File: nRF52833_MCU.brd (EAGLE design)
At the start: 47.7 x 30.2 mm, 45 parts, among them IC1 SKY13415-485LF, J100 DEBUG_CONNECTOR, J3 282834-2, U1 nRF52833-QIAA, X1 32MHz, X2 32.768kHz, X3 22-23-2031

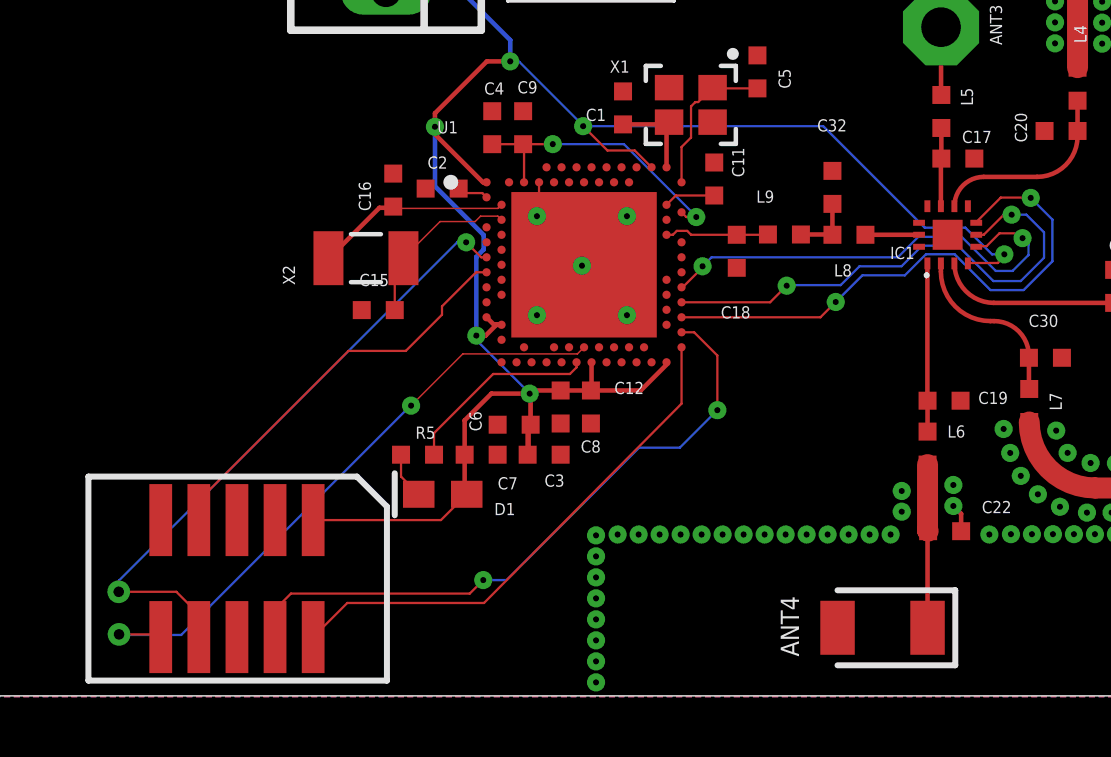
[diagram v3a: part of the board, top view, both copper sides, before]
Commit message: Disconnect reset
Signed-off-by: Florian Depraz <florian.depraz@outlook.com>
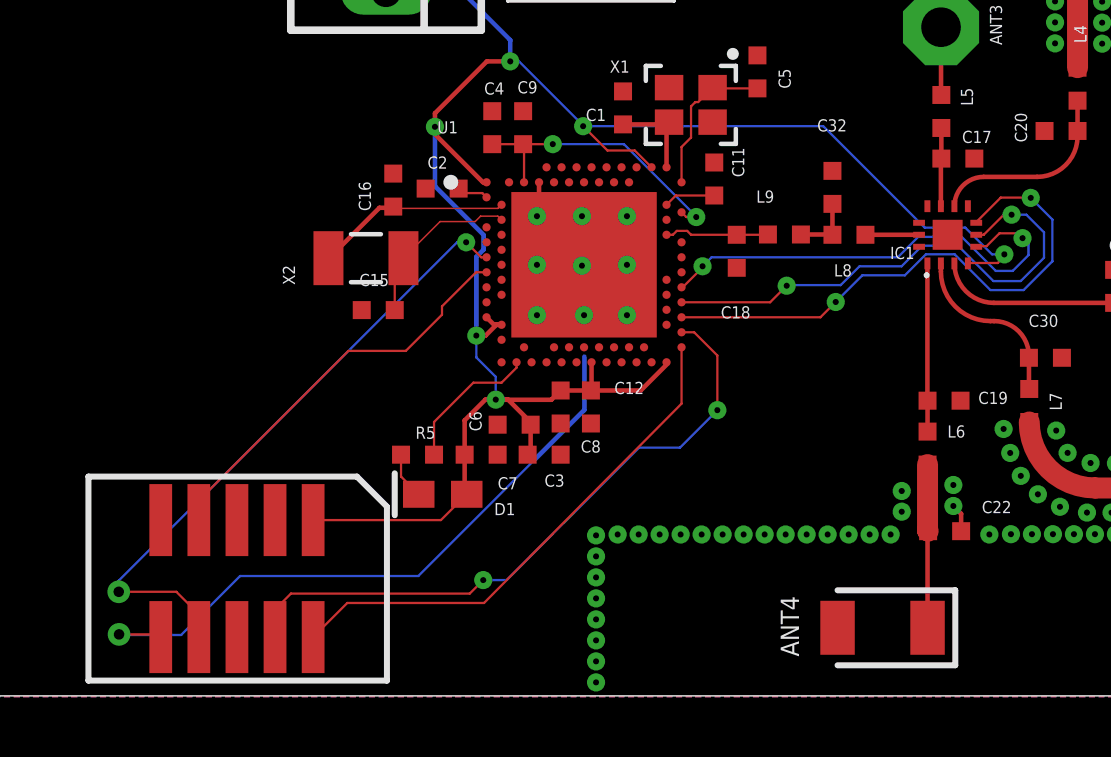
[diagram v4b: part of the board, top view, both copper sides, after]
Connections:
- net LED1: now also U1.AD4; no longer U1.AD12
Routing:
- net GND: track 3.13 -> 5.27 mm, vias 39 -> 43
- net VDD: track 68.9 -> 67.1 mm
- net LED1: track 6.55 -> 4.77 mm
- net RESET: track 20.9 -> 21.8 mm, vias 2 -> 1
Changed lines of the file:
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@@
 <signal name="LED1">
 <contactref element="R5" pad="1"/>
-<contactref element="U1" pad="AD12"/>
-<wire x1="30.07" y1="39.55" x2="30.07" y2="40.27" width="0.0762" layer="1"/>
-<wire x1="34.82" y1="42.63" x2="34.82" y2="42.46" width="0.0762" layer="1"/>
-<wire x1="34.82" y1="42.46" x2="34.6" y2="42.24" width="0.0762" layer="1"/>
-<wire x1="32.04" y1="42.24" x2="30.07" y2="40.27" width="0.0762" layer="1"/>
-<wire x1="34.6" y1="42.24" x2="32.04" y2="42.24" width="0.0762" layer="1"/>
+<wire x1="30.07" y1="39.55" x2="30.07" y2="40.64" width="0.0762" layer="1"/>
+<wire x1="31.38" y1="41.95" x2="30.07" y2="40.64" width="0.0762" layer="1"/>
+<wire x1="32.32" y1="41.95" x2="31.38" y2="41.95" width="0.0762" layer="1"/>
+<contactref element="U1" pad="AD4"/>
+<wire x1="32.820003125" y1="42.63" x2="32.820003125" y2="42.450003125" width="0.0762" layer="1"/>
+<wire x1="32.820003125" y1="42.450003125" x2="32.32" y2="41.95" width="0.0762" layer="1"/>
 </signal>
 <signal name="P0.07_RX">
@@
 <wire x1="35.04" y1="50.52" x2="32.91" y2="52.65" width="0.0762" layer="16"/>
 <via x="35.04" y="50.5" extent="1-16" drill="0.2"/>
-<wire x1="33.19" y1="39.55" x2="33.26" y2="39.62" width="0.0762" layer="1"/>
-<wire x1="33.2575" y1="41.5857" x2="33.26" y2="41.5832" width="0.0762" layer="1"/>
-<wire x1="33.26" y1="41.5832" x2="33.26" y2="39.62" width="0.0762" layer="1"/>
-<via x="33.2575" y="41.5857" extent="1-16" drill="0.2"/>
+<via x="32.1275" y="41.3857" extent="1-16" drill="0.2"/>
 <wire x1="37.820003125" y1="42.63" x2="37.820003125" y2="42.55" width="0.0762" layer="1"/>
 <wire x1="36.960003125" y1="41.69" x2="37.820003125" y2="42.55" width="0.1524" layer="1"/>
@@
 <contactref element="U1" pad="Y2"/>
 <via x="32.61" y="52.66" extent="1-16" drill="0.2"/>
-<wire x1="31.98190625" y1="41.5857" x2="33.2575" y2="41.5857" width="0.1524" layer="1"/>
+<wire x1="31.78190625" y1="41.3857" x2="32.1275" y2="41.3857" width="0.1524" layer="1"/>
 <wire x1="31.09" y1="39.55" x2="31.09" y2="40.69379375" width="0.1524" layer="1"/>
-<wire x1="31.09" y1="40.69379375" x2="31.98190625" y2="41.5857" width="0.1524" layer="1"/>
+<wire x1="31.09" y1="40.69379375" x2="31.78190625" y2="41.3857" width="0.1524" layer="1"/>
 <wire x1="35.320003125" y1="41.710003125" x2="35.320003125" y2="42.63" width="0.1524" layer="1"/>
 <wire x1="31.09" y1="39.55" x2="31.09" y2="38.3" width="0.1524" layer="1"/>
@@
 <wire x1="30.3" y1="37.37" x2="26.04" y2="37.37" width="0.0762" layer="1"/>
 <via x="31.479328125" y="43.520671875" extent="1-16" drill="0.2"/>
-<wire x1="33.2575" y1="41.5857" x2="33.2575" y2="41.5957" width="0.0762" layer="16"/>
-<wire x1="33.2575" y1="41.5957" x2="31.479328125" y2="43.373871875" width="0.0762" layer="16"/>
-<wire x1="31.479328125" y1="43.373871875" x2="31.479328125" y2="43.5" width="0.0762" layer="16"/>
+<wire x1="32.1275" y1="41.3857" x2="32.1275" y2="42.1457" width="0.0762" layer="16"/>
+<wire x1="32.1275" y1="42.1457" x2="31.479328125" y2="42.793871875" width="0.0762" layer="16"/>
+<wire x1="31.479328125" y1="42.793871875" x2="31.479328125" y2="43.5" width="0.0762" layer="16"/>
 <wire x1="31.479328125" y1="43.5" x2="31.479328125" y2="43.520671875" width="0.0762" layer="16"/>
 <wire x1="31.7244" y1="46.87206875" x2="31.7244" y2="46.38793125" width="0.1524" layer="16"/>
@@
 <wire x1="31.479328125" y1="46.142859375" x2="31.479328125" y2="43.5" width="0.1524" layer="16"/>
 <wire x1="32.61" y1="53.37" x2="32.61" y2="52.66" width="0.1524" layer="16"/>
-<wire x1="33.19" y1="39.55" x2="33.19" y2="40.45" width="0.1524" layer="1"/>
-<wire x1="33.19" y1="40.45" x2="33.29" y2="40.55" width="0.1524" layer="1"/>
-<wire x1="33.29" y1="40.55" x2="33.29" y2="41.5532" width="0.1524" layer="1"/>
-<wire x1="33.29" y1="41.5532" x2="33.2575" y2="41.5857" width="0.1524" layer="1"/>
+<wire x1="33.29" y1="40.55" x2="33.29" y2="39.65" width="0.1524" layer="1"/>
+<wire x1="33.29" y1="39.65" x2="33.19" y2="39.55" width="0.1524" layer="1"/>
+<wire x1="33.29" y1="40.55" x2="33.29" y2="40.6332" width="0.1524" layer="1"/>
+<wire x1="33.29" y1="40.6332" x2="32.5375" y2="41.3857" width="0.1524" layer="1"/>
+<wire x1="32.5375" y1="41.3857" x2="32.1275" y2="41.3857" width="0.1524" layer="1"/>
 <wire x1="32.32" y1="43.88" x2="32.14786875" y2="43.88" width="0.1524" layer="1"/>
 <wire x1="31.788540625" y1="43.520671875" x2="31.479328125" y2="43.520671875" width="0.1524" layer="1"/>
@@
 <wire x1="32.32" y1="43.88" x2="32.069996875" y2="43.88" width="0.1524" layer="1"/>
 <wire x1="32.069996875" y1="43.88" x2="31.82" y2="44.129996875" width="0.1524" layer="1"/>
-<wire x1="33.2575" y1="41.5857" x2="33.3618" y2="41.69" width="0.1524" layer="1"/>
-<wire x1="33.3618" y1="41.69" x2="34.29" y2="41.69" width="0.1524" layer="1"/>
+<wire x1="33.98" y1="41.38" x2="32.1332" y2="41.38" width="0.1524" layer="1"/>
+<wire x1="32.1275" y1="41.3857" x2="32.1332" y2="41.38" width="0.1524" layer="1"/>
+<wire x1="33.98" y1="41.38" x2="34.29" y2="41.69" width="0.1524" layer="1"/>
 <wire x1="34.29" y1="41.69" x2="35.3" y2="41.69" width="0.1524" layer="1"/>
 <wire x1="35.3" y1="41.69" x2="35.320003125" y2="41.710003125" width="0.1524" layer="1"/>
@@
 <via x="43.46" y="44.64" extent="1-16" drill="0.2"/>
 <wire x1="49.96" y1="48.11" x2="50.6837" y2="47.3863" width="0.0762" layer="16"/>
-<wire x1="43.46" y1="44.64" x2="43.45" y2="44.63" width="0.0762" layer="1"/>
 <wire x1="50.6837" y1="45.99673125" x2="49.72376875" y2="45.0368" width="0.0762" layer="16"/>
 <wire x1="49.72376875" y1="45.0368" x2="48.6178375" y2="45.0368" width="0.0762" layer="16"/>
@@
 <contactref element="U1" pad="W24"/>
 <wire x1="38.32" y1="44.129996875" x2="42.949996875" y2="44.129996875" width="0.0762" layer="1"/>
-<wire x1="42.949996875" y1="44.129996875" x2="43.46" y2="44.64" width="0.0762" layer="1"/>
+<wire x1="43.46" y1="44.64" x2="42.949996875" y2="44.129996875" width="0.0762" layer="1"/>
 </signal>
 <signal name="ANT_SEL_V2">
@@
 <via x="41.825" y="45.1825" extent="1-16" drill="0.2"/>
 <via x="49.3225" y="47.55" extent="1-16" drill="0.2"/>
-<wire x1="41.825" y1="45.1825" x2="41.7525" y2="45.11" width="0.0762" layer="1"/>
 <wire x1="46.34" y1="46.516159375" x2="47.536159375" y2="46.516159375" width="0.0762" layer="16"/>
 <wire x1="47.536159375" y1="46.516159375" x2="48.71431875" y2="45.338" width="0.0762" layer="16"/>
@@
 <contactref element="U1" pad="U24"/>
 <wire x1="38.32" y1="44.63" x2="41.2725" y2="44.63" width="0.0762" layer="1"/>
-<wire x1="41.2725" y1="44.63" x2="41.825" y2="45.1825" width="0.0762" layer="1"/>
+<wire x1="41.825" y1="45.1825" x2="41.2725" y2="44.63" width="0.0762" layer="1"/>
 </signal>
 <signal name="ANT_SEL_V3">
@@
 </signal>
 <signal name="RESET">
-<contactref element="U1" pad="AC13"/>
 <contactref element="J100" pad="10"/>
-<wire x1="35.07" y1="43.129996875" x2="34.84910625" y2="42.909103125" width="0.05" layer="1"/>
-<wire x1="34.84910625" y1="42.909103125" x2="31.029390625" y2="42.909390625" width="0.05" layer="1"/>
-<wire x1="31.029390625" y1="42.909390625" x2="29.305" y2="41.185" width="0.05" layer="1"/>
-<via x="29.305" y="41.185" extent="1-16" drill="0.2"/>
-<wire x1="29.305" y1="41.185" x2="29.285" y2="41.185" width="0.0762" layer="16"/>
-<wire x1="29.285" y1="41.185" x2="21.64" y2="33.54" width="0.0762" layer="16"/>
+<wire x1="23.605" y1="35.505" x2="21.64" y2="33.54" width="0.0762" layer="16"/>
 <wire x1="21.64" y1="33.54" x2="19.57" y2="33.54" width="0.0762" layer="16"/>
 <wire x1="19.57" y1="33.54" x2="19.57" y2="33.56" width="0.0762" layer="16"/>
@@
 <wire x1="19.57" y1="33.56" x2="20.87" y2="33.56" width="0.0762" layer="1"/>
 <wire x1="20.87" y1="33.56" x2="20.96" y2="33.47" width="0.0762" layer="1"/>
+<wire x1="29.545" y1="35.505" x2="23.605" y2="35.505" width="0.0762" layer="16"/>
+<wire x1="29.545" y1="35.505" x2="33.43" y2="39.39" width="0.0762" layer="16"/>
+<contactref element="U1" pad="AC13"/>
+<wire x1="33.43" y1="39.39" x2="35.08" y2="41.04" width="0.1524" layer="16"/>
+<wire x1="35.08" y1="41.04" x2="35.08" y2="42.82" width="0.1524" layer="16"/>
+<wire x1="35.08" y1="42.82" x2="35.07" y2="43.129996875" width="0" layer="19" extent="1-16"/>
 </signal>
 <signal name="DEC1">
@@
 <contactref element="L6" pad="2"/>
 <contactref element="C22" pad="1"/>
-<wire x1="46.52" y1="39.22" x2="46.5456125" y2="39.1943875" width="0.1524" layer="1"/>
 <wire x1="46.52" y1="39.22" x2="46.52" y2="37.02" width="0.7" layer="1"/>
 <wire x1="46.52" y1="37.02" x2="46.54" y2="37" width="0.7" layer="1"/>
@@
 <wire x1="57.17" y1="51.91" x2="57.17" y2="52.61" width="0" layer="19" extent="1-1"/>
 </signal>
-<signal name="GND" class="1">
+<signal name="GND">
 <contactref element="C18" pad="2"/>
 <contactref element="C32" pad="2"/>
@@
 <via x="36.5" y="44.2" extent="1-16" drill="0.2"/>
 <via x="33.5" y="44.2" extent="1-16" drill="0.2"/>
-<wire x1="33.57" y1="48.63" x2="33.57" y2="47.47" width="0.0762" layer="1"/>
-<wire x1="33.57" y1="47.47" x2="33.5" y2="47.5" width="0.0762" layer="1"/>
 <wire x1="52.34000625" y1="55.35" x2="52.34000625" y2="55.90000625" width="0.1524" layer="1"/>
 <wire x1="52.34000625" y1="55.90000625" x2="52.62" y2="56.18" width="0.1524" layer="1"/>
@@
 <wire x1="47.64" y1="37" x2="47.640028125" y2="37.000028125" width="0.1524" layer="1"/>
 <wire x1="47.640028125" y1="37.58" x2="47.380028125" y2="37.84" width="0.1524" layer="1"/>
+<via x="35" y="47.5" extent="1-16" drill="0.2"/>
+<via x="33.5" y="45.88" extent="1-16" drill="0.2"/>
+<via x="35.07" y="44.2" extent="1-16" drill="0.2"/>
+<via x="36.5" y="45.88" extent="1-16" drill="0.2"/>
+<wire x1="35.07" y1="45.88" x2="33.57" y2="47.38" width="0.1524" layer="1"/>
+<wire x1="33.57" y1="47.38" x2="33.57" y2="48.63" width="0.1524" layer="1"/>
 </signal>
 <signal name="N$22">

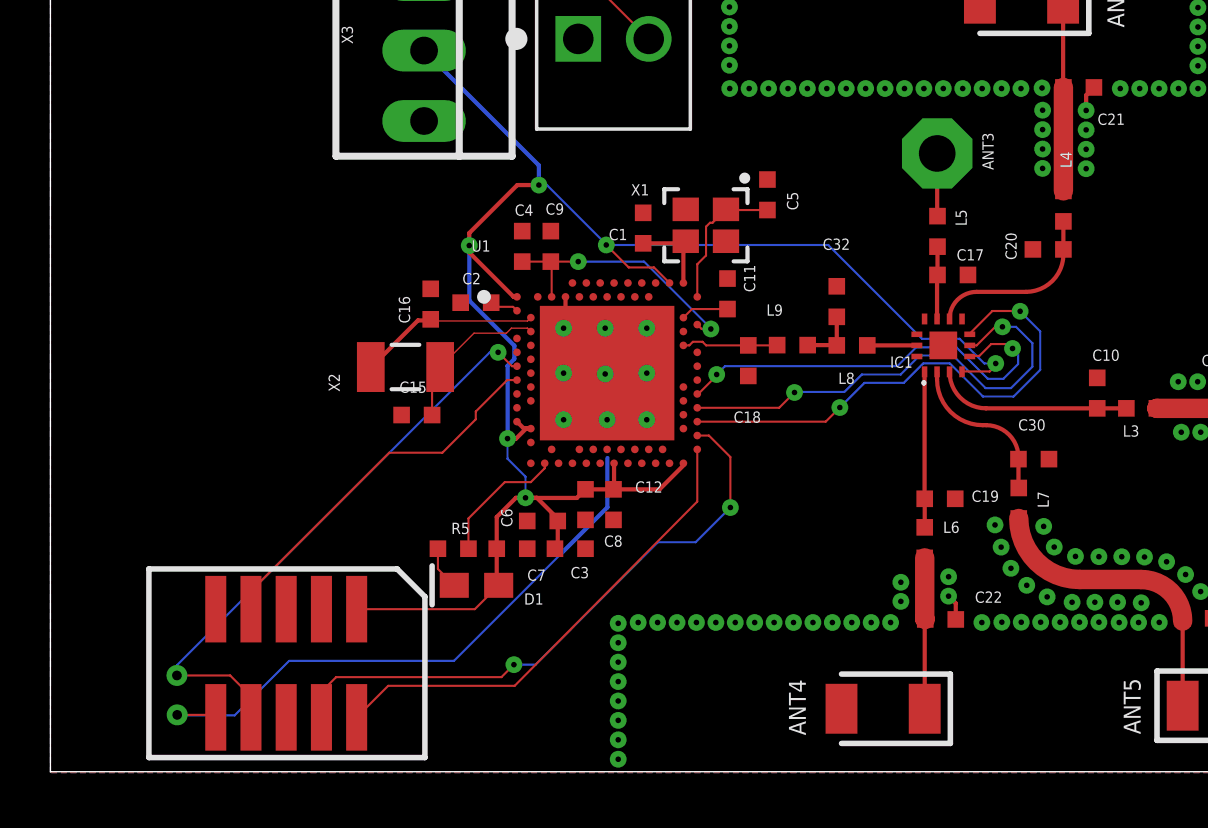
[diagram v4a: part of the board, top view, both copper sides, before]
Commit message: Reduce signal size
Signed-off-by: Florian Depraz <florian.depraz@outlook.com>
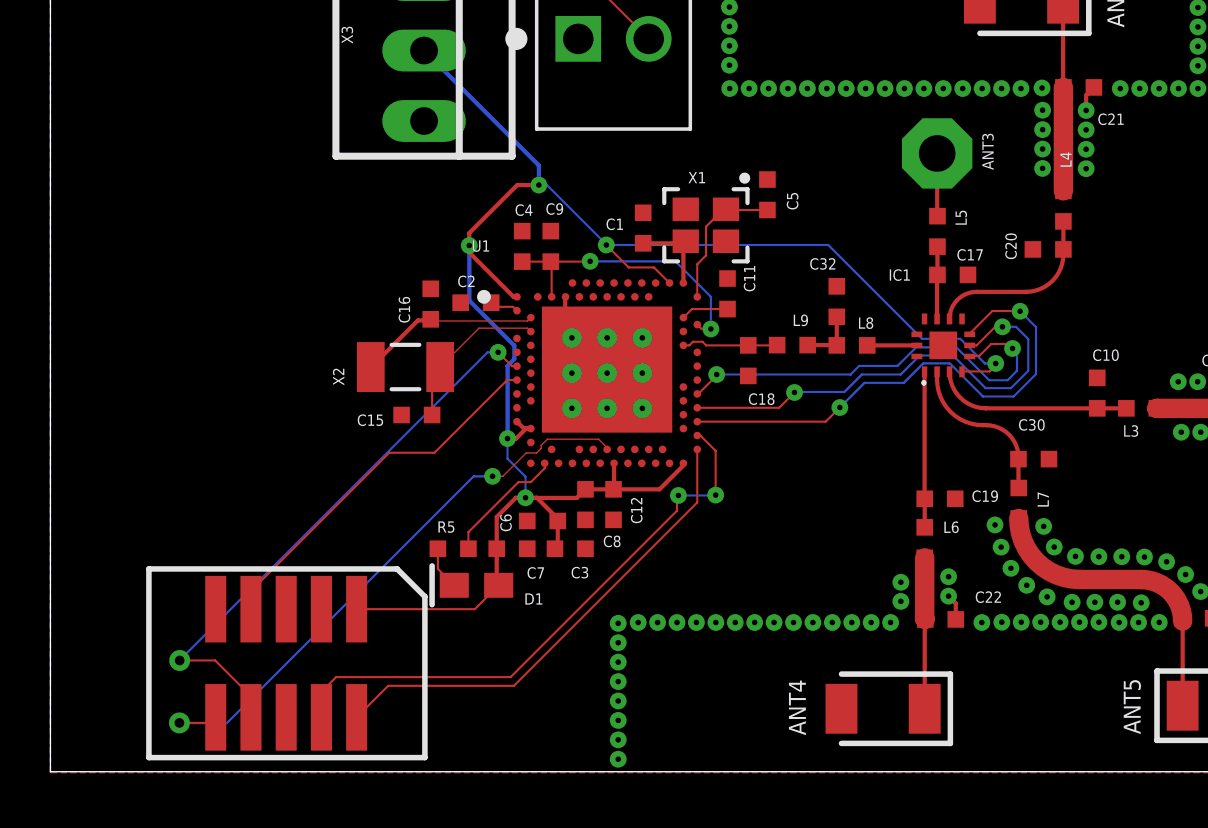
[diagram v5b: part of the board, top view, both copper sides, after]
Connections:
- net GND: now also U1.P$1, U1.P$2, U1.P$3, U1.P$4, U1.P$5, U1.P$6, U1.P$7, U1.P$8, U1.P$9
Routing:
- net GND: track 5.27 -> 3.38 mm, vias 43 -> 34
- net SWDCLK: track 21.8 -> 20.9 mm
- net DEC6: track 9.66 -> 10.3 mm
- net RESET: track 21.8 -> 21.3 mm, vias 1 -> 2

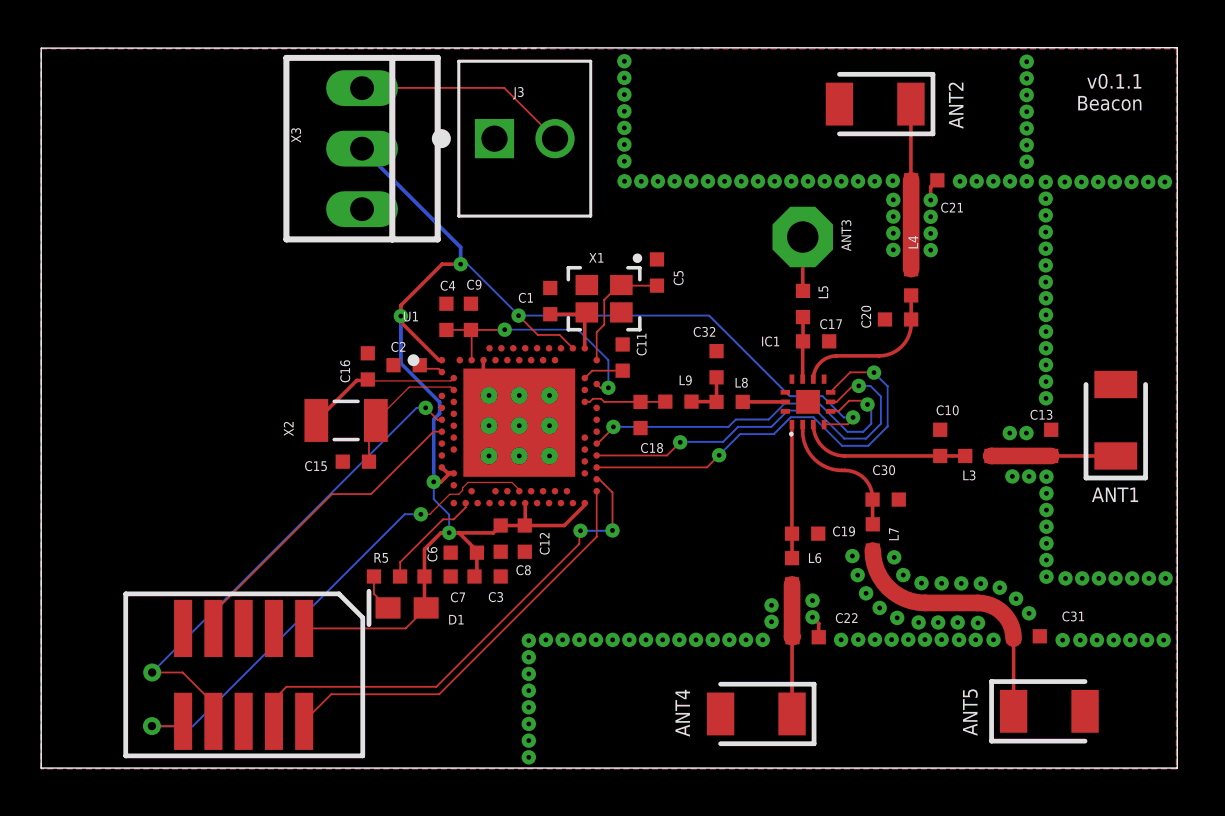
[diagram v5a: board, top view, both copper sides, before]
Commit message: Increase some signal size
Signed-off-by: Florian Depraz <florian.depraz@outlook.com>
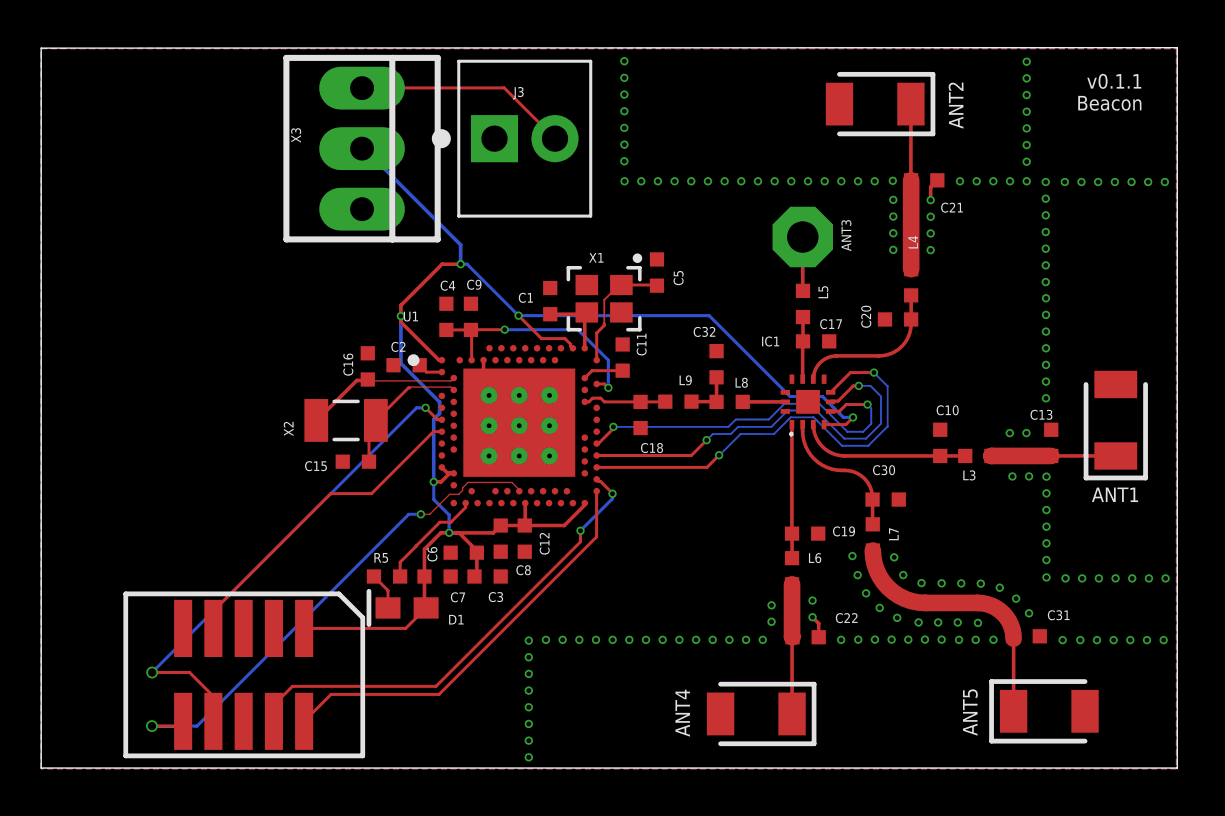
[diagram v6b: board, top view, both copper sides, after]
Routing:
- net SWDCLK: track 20.9 -> 19.9 mm
